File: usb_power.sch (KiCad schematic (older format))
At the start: 54 parts, among them J1 M20-8770642R, J2 USB_B_Micro, J3 M20-8770642R, Q1 IRLML6402, Q2 BSS214NW, U1 FT230XS, U2 MCP1726-3302ESN, U3 MIC5319-1.8YD5-TR

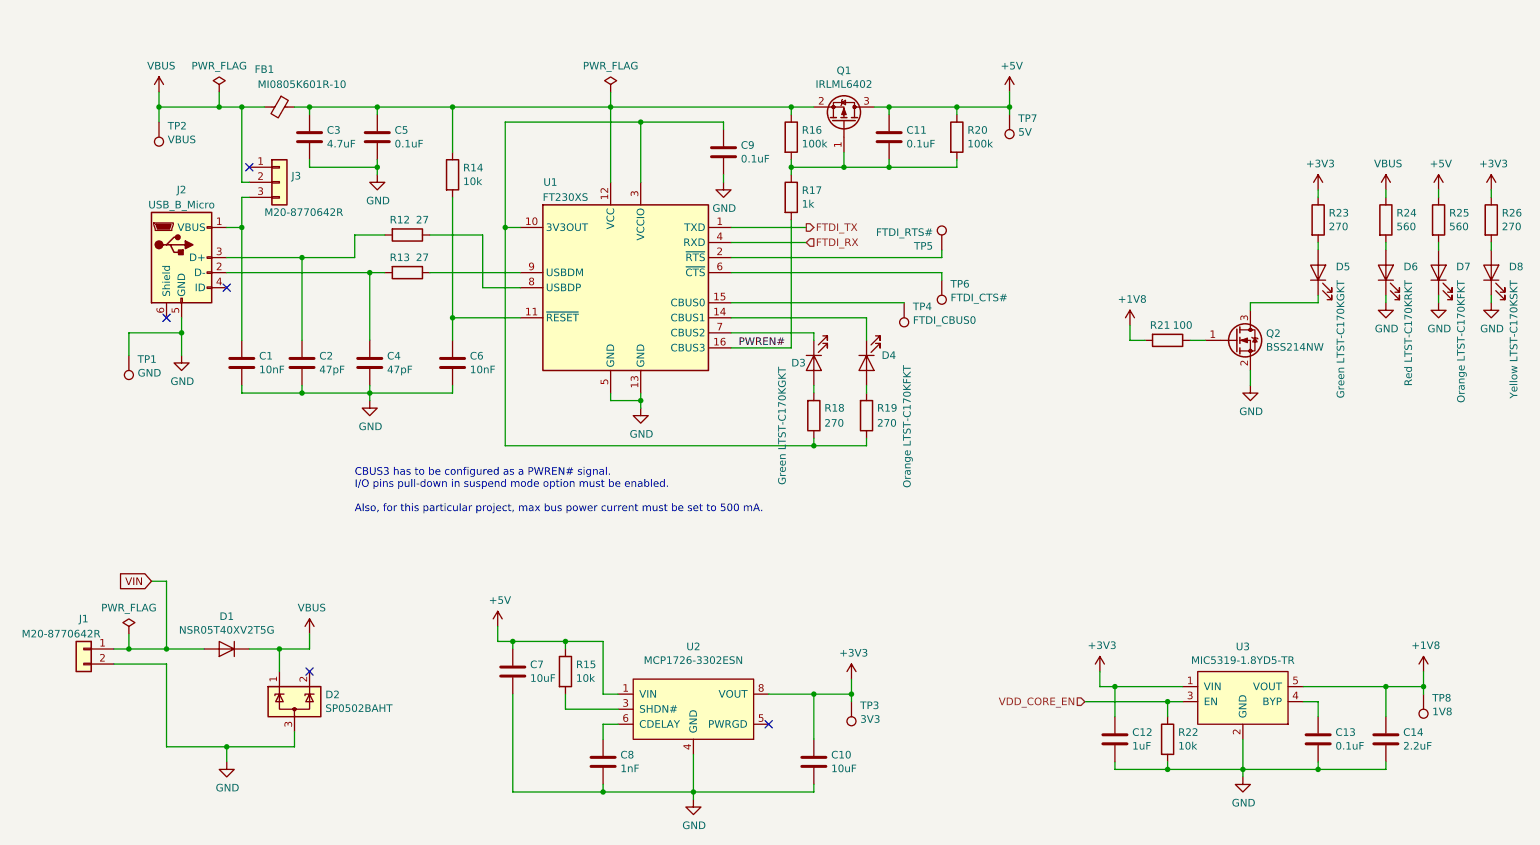
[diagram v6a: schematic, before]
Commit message: Placed pressure sensor, connector changed to USB-C
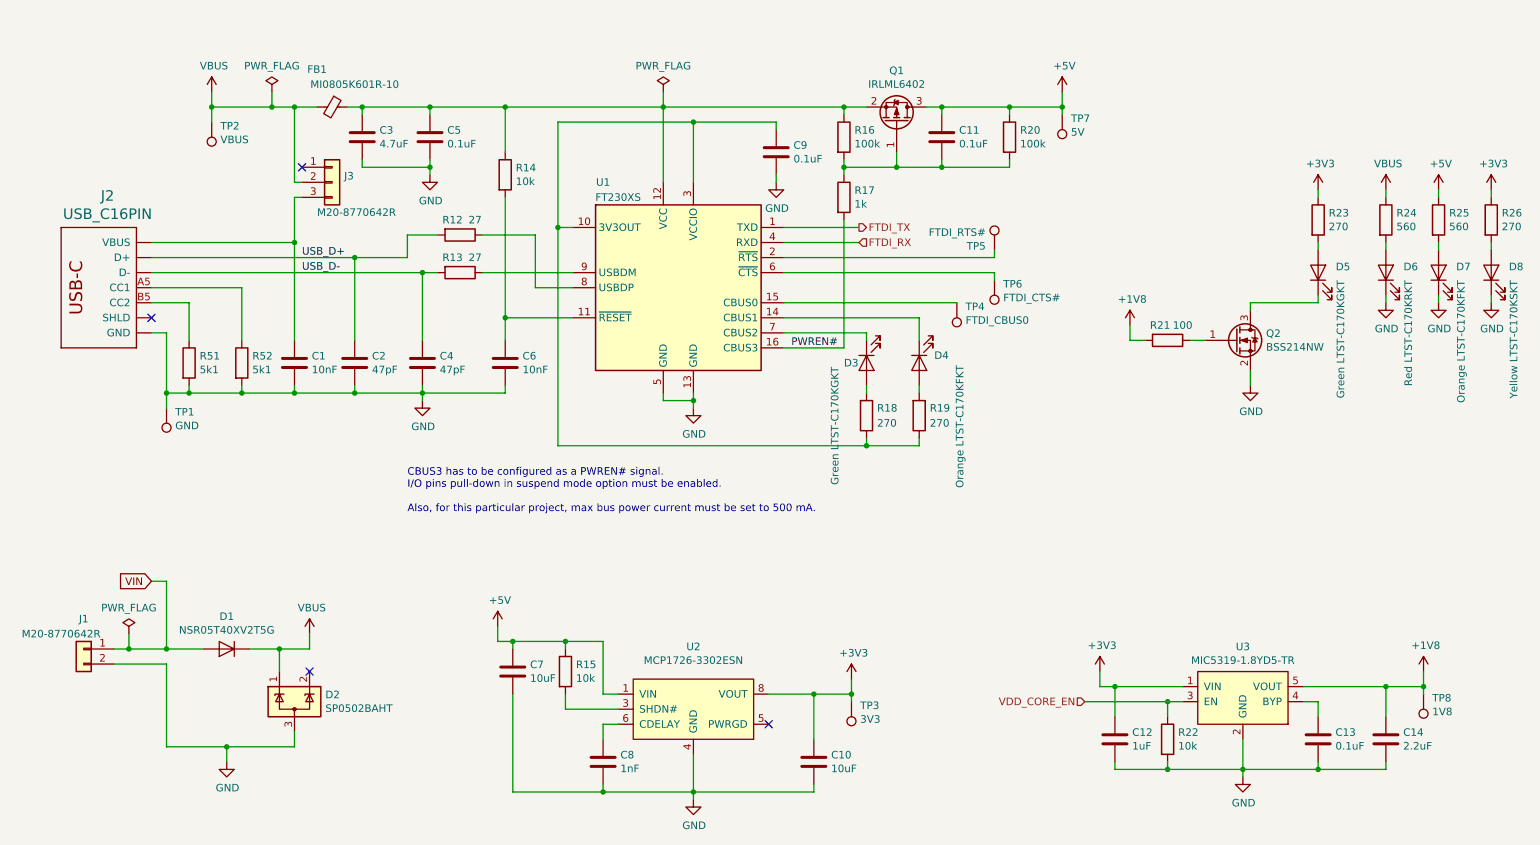
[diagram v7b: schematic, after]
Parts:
- removed J2: USB_B_Micro, Connector_USB:USB_Micro-B_Molex-105017-0001, symbol Connector:USB_B_Micro
- added J2: USB_C16PIN, USB-C-16pin:USB-C-COM-15111, symbol USB-C-16pin:USB_C16PIN
- added R51, R52: 5k1, Resistor_SMD:R_0805_2012Metric_Pad1.15x1.40mm_HandSolder, symbol Device:R
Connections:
- net GND: now also J2.GND, J2.GND2 (GND), R51.2, R52.2
- net at C1.1, J3.3 (Pin_3): now also J2.VBUS1 (VBUS), J2.VBUS2 (VBUS)
- net USB_D-: now reaches C4.1, R13.2
- net USB_D-: now also J2.A7 (D-), J2.B7 (D-)
- net USB_D+: now reaches C2.1, R12.2
- net USB_D+: now also J2.A6 (D+), J2.B6 (D+)
- new net: J2.A5 (CC1), R52.1
- new net: J2.B5 (CC2), R51.1
- new net: J2.SHLD1 (SHLD), J2.SHLD2 (SHLD), J2.SHLD3 (SHLD), J2.SHLD4 (SHLD), J2.SHLD5 (SHLD), J2.SHLD6 (SHLD), J2.SHLD7 (SHLD), J2.SHLD8 (SHLD)
- no-connect marks 5 -> 4
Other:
- moved on the sheet: C1, C11, C2, C3, C4, C5, C6, C9, D3, D4, FB1, J3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

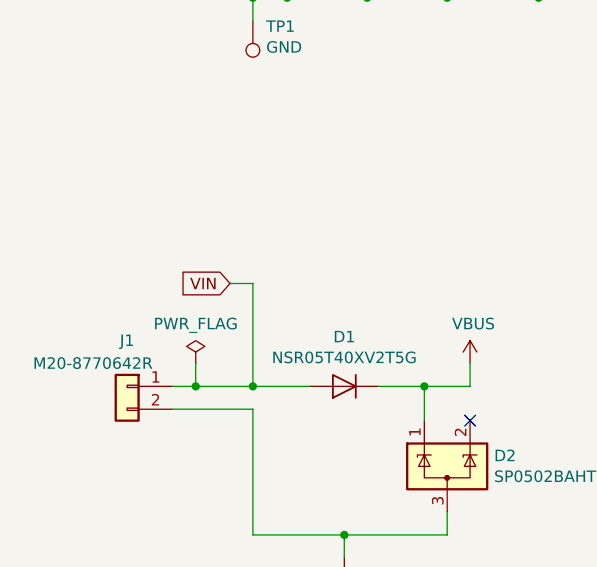
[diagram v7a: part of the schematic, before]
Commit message: Route power traces on the inner layer
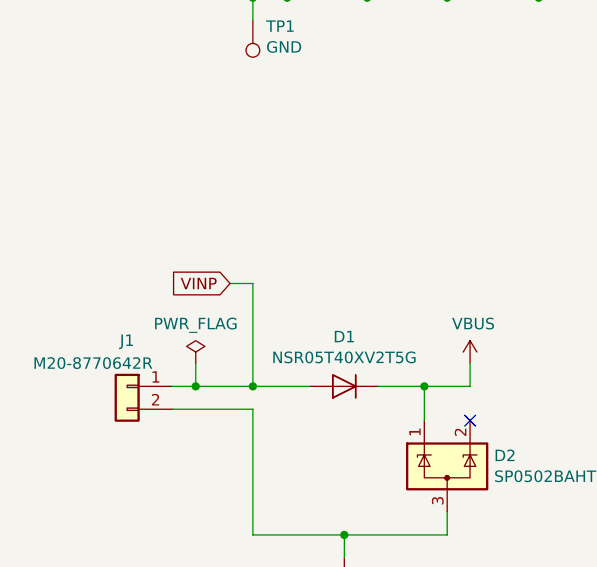
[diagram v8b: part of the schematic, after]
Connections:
- net +5V: no longer D1.2 (A), J1.1 (Pin_1)
- new net VINP: D1.2 (A), J1.1 (Pin_1)
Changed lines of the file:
@@
 	8650 2650 8650 2700
 Text GLabel 1350 4500 0    50   Input ~ 0
-VIN
+VINP
 Wire Wire Line
 	1100 4950 1200 4950
